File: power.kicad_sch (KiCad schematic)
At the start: 103 parts, among them Q1 BSS138AKA, Q2 SQS401EN-T1_BE3, Q3 DZDH0401DW, Q4 DMG1012T-7, Q5 DMG1012T-7, U3 LMR62014XMF, U4 AP62301_TSOT, U5 AP62301_TSOT, U6 AP22615A_TSOT26

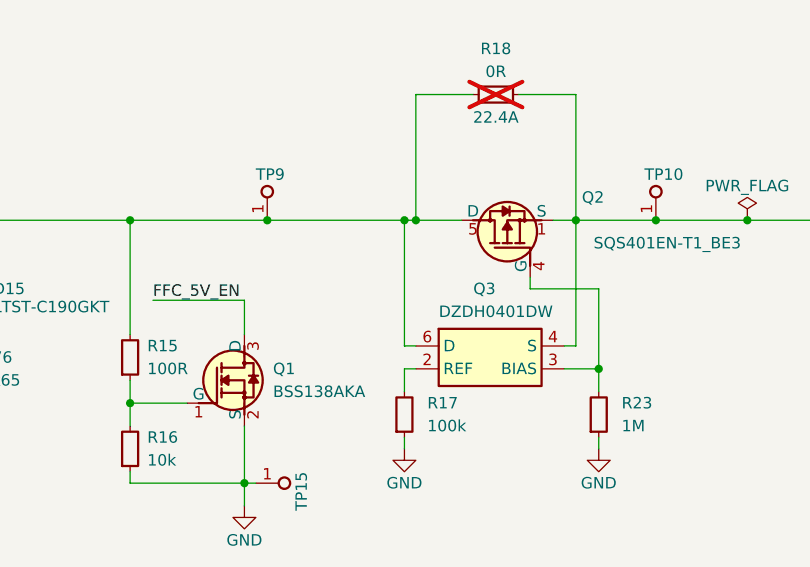
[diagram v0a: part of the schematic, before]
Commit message: [#74135] Update symbols and footprints
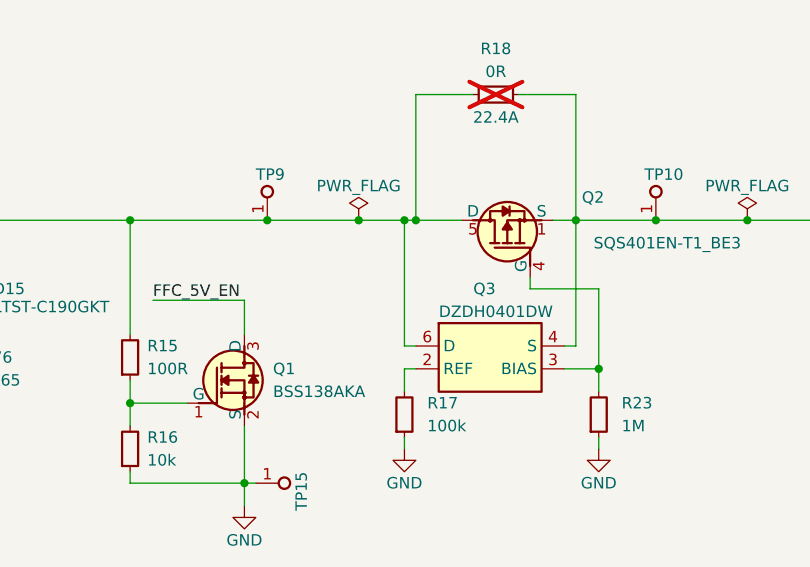
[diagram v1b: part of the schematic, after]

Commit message: [#74135] Fix DNP malformations
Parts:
- R18, R34: DNP DNP -> (none)
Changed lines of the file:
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@@
 			)
 		)
-		(property "DNP" "DNP"
-			(at 309.88 227.33 0)
-			(effects
-				(font
-					(size 1.27 1.27)
-				)
-				(hide yes)
-			)
-		)
 		(pin "1"
 		)
@@
 				(hide yes)
 			)
-		)
-		(property "DNP" "DNP"
-			(at 91.44 210.82 0)
-			(effects
-				(font
-					(size 1.27 1.27)
-				)
-				(hide yes)
-			)

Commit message: [#74135] Clean noInBom fields
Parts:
- Q4, Q5: now in the parts list
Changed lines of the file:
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@@
 	(label "FB_1V8"
 		(at 309.88 66.04 0)
-		(fields_autoplaced yes)
 		(effects
 			(font
@@
 	(label "FB_1V2"
 		(at 309.88 142.24 0)
-		(fields_autoplaced yes)
 		(effects
 			(font
@@
 	(label "EN_1V2"
 		(at 280.67 137.16 0)
-		(fields_autoplaced yes)
 		(effects
 			(font
@@
 	(label "FFC_5V_EN"
 		(at 347.98 222.25 0)
-		(fields_autoplaced yes)
 		(effects
 			(font
@@
 	(label "OUT_1V8"
 		(at 367.03 71.12 0)
-		(fields_autoplaced yes)
 		(effects
 			(font
@@
 	(label "FFC_5V_ISET"
 		(at 374.65 219.71 0)
-		(fields_autoplaced yes)
 		(effects
 			(font
@@
 	(label "SW_1V8"
 		(at 309.88 55.88 0)
-		(fields_autoplaced yes)
 		(effects
 			(font
@@
 	(label "EN_12V"
 		(at 189.23 238.76 0)
-		(fields_autoplaced yes)
 		(effects
 			(font
@@
 	(label "OUT_12V"
 		(at 238.76 232.41 0)
-		(fields_autoplaced yes)
 		(effects
 			(font
@@
 	(label "OUT_12V"
 		(at 275.59 240.03 270)
-		(fields_autoplaced yes)
 		(effects
 			(font
@@
 	(label "OUT_1V2"
 		(at 367.03 152.4 0)
-		(fields_autoplaced yes)
 		(effects
 			(font
@@
 	(label "EN_1V8"
 		(at 280.67 60.96 0)
-		(fields_autoplaced yes)
 		(effects
 			(font
@@
 	(label "FFC_5V_EN"
 		(at 326.39 223.52 180)
-		(fields_autoplaced yes)
 		(effects
 			(font
@@
 	(label "OUT_1V8"
 		(at 340.36 55.88 0)
-		(fields_autoplaced yes)
 		(effects
 			(font
@@
 	(label "SW_12V"
 		(at 214.63 232.41 0)
-		(fields_autoplaced yes)
 		(effects
 			(font
@@
 	(label "FB_12V"
 		(at 214.63 237.49 0)
-		(fields_autoplaced yes)
 		(effects
 			(font
@@
 	(label "OUT_1V2"
 		(at 340.36 132.08 0)
-		(fields_autoplaced yes)
 		(effects
 			(font
@@
 	(label "FFC_5V_EN"
 		(at 53.34 233.68 0)
-		(fields_autoplaced yes)
 		(effects
 			(font
@@
 	(label "SW_1V2"
 		(at 309.88 132.08 0)
-		(fields_autoplaced yes)
 		(effects
 			(font
@@
 	(label "FFC_5V_FLG"
 		(at 347.98 219.71 0)
-		(fields_autoplaced yes)
 		(effects
 			(font
@@
 		(shape input)
 		(at 330.2 217.17 180)
-		(fields_autoplaced yes)
 		(effects
 			(font
@@
 		(shape output)
 		(at 168.91 62.23 0)
-		(fields_autoplaced yes)
 		(effects
 			(font
@@
 		(shape input)
 		(at 309.88 215.9 90)
-		(fields_autoplaced yes)
 		(effects
 			(font
@@
 		(shape input)
 		(at 30.48 224.79 180)
-		(fields_autoplaced yes)
 		(effects
 			(font
@@
 		(shape output)
 		(at 168.91 140.97 0)
-		(fields_autoplaced yes)
 		(effects
 			(font
@@
 		(shape output)
 		(at 168.91 88.9 0)
-		(fields_autoplaced yes)
 		(effects
 			(font
@@
 		(shape output)
 		(at 168.91 114.3 0)
-		(fields_autoplaced yes)
 		(effects
 			(font
@@
 		(unit 1)
 		(exclude_from_sim no)
-		(in_bom no)
+		(in_bom yes)
 		(on_board yes)
 		(dnp no)
@@
 		(unit 1)
 		(exclude_from_sim no)
-		(in_bom no)
+		(in_bom yes)
 		(on_board yes)
 		(dnp no)

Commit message: [#80514] change 59S2AQ-40MT5-Z_1 connector to 7-2287906-0
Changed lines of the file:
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@@
 (kicad_sch
-	(version 20231120)
+	(version 20250114)
 	(generator "eeschema")
-	(generator_version "8.0")
+	(generator_version "9.0")
 	(paper "A3")
 	(title_block
@@
 		(comment 1 "www.antmicro.com")
 	)
+	(text "FFC 5V current limit"
+		(exclude_from_sim no)
+		(at 323.85 187.96 0)
+		(effects
+			(font
+				(size 4 4)
+				(thickness 0.8)
+				(bold yes)
+			)
+			(justify left bottom)
+		)
+	)
+	(text "Power arbiter"
+		(exclude_from_sim no)
+		(at 56.515 189.865 0)
+		(effects
+			(font
+				(size 4 4)
+				(thickness 0.8)
+				(bold yes)
+			)
+			(justify left bottom)
+		)
+	)
+	(text "Buck converter\n12V to 1.8V"
+		(exclude_from_sim no)
+		(at 294.64 28.575 0)
+		(effects
+			(font
+				(size 4 4)
+				(thickness 0.8)
+				(bold yes)
+			)
+			(justify left bottom)
+		)
+	)
+	(text "Boost converter\n5V to 12V"
+		(exclude_from_sim no)
+		(at 191.135 194.945 0)
+		(effects
+			(font
+				(size 4 4)
+				(thickness 0.8)
+				(bold yes)
+			)
+			(justify left bottom)
+		)
+	)
+	(text "Buck converter\n12V to 1.2V"
+		(exclude_from_sim no)
+		(at 294.64 105.41 0)
+		(effects
+			(font
+				(size 4 4)
+				(thickness 0.8)
+				(bold yes)
+			)
+			(justify left bottom)
+		)
+	)
+	(text "PoC circuit"
+		(exclude_from_sim no)
+		(at 94.615 37.465 0)
+		(effects
+			(font
+				(size 4 4)
+				(thickness 0.8)
+				(bold yes)
+			)
+			(justify left bottom)
+		)
+	)
 	(junction
 		(at 320.04 132.08)
@@
 		)
 	)
-	(text "FFC 5V current limit"
-		(exclude_from_sim no)
-		(at 323.85 187.96 0)
-		(effects
-			(font
-				(size 4 4)
-				(thickness 0.8)
-				(bold yes)
-			)
-			(justify left bottom)
-		)
-	)
-	(text "Power arbiter"
-		(exclude_from_sim no)
-		(at 56.515 189.865 0)
-		(effects
-			(font
-				(size 4 4)
-				(thickness 0.8)
-				(bold yes)
-			)
-			(justify left bottom)
-		)
-	)
-	(text "Buck converter\n12V to 1.8V"
-		(exclude_from_sim no)
-		(at 294.64 28.575 0)
-		(effects
-			(font
-				(size 4 4)
-				(thickness 0.8)
-				(bold yes)
-			)
-			(justify left bottom)
-		)
-	)
-	(text "Boost converter\n5V to 12V"
-		(exclude_from_sim no)
-		(at 191.135 194.945 0)
-		(effects
-			(font
-				(size 4 4)
-				(thickness 0.8)
-				(bold yes)
-			)
-			(justify left bottom)
-		)
-	)
-	(text "Buck converter\n12V to 1.2V"
-		(exclude_from_sim no)
-		(at 294.64 105.41 0)
-		(effects
-			(font
-				(size 4 4)
-				(thickness 0.8)
-				(bold yes)
-			)
-			(justify left bottom)
-		)
-	)
-	(text "PoC circuit"
-		(exclude_from_sim no)
-		(at 94.615 37.465 0)
-		(effects
-			(font
-				(size 4 4)
-				(thickness 0.8)
-				(bold yes)
-			)
-			(justify left bottom)
-		)
-	)

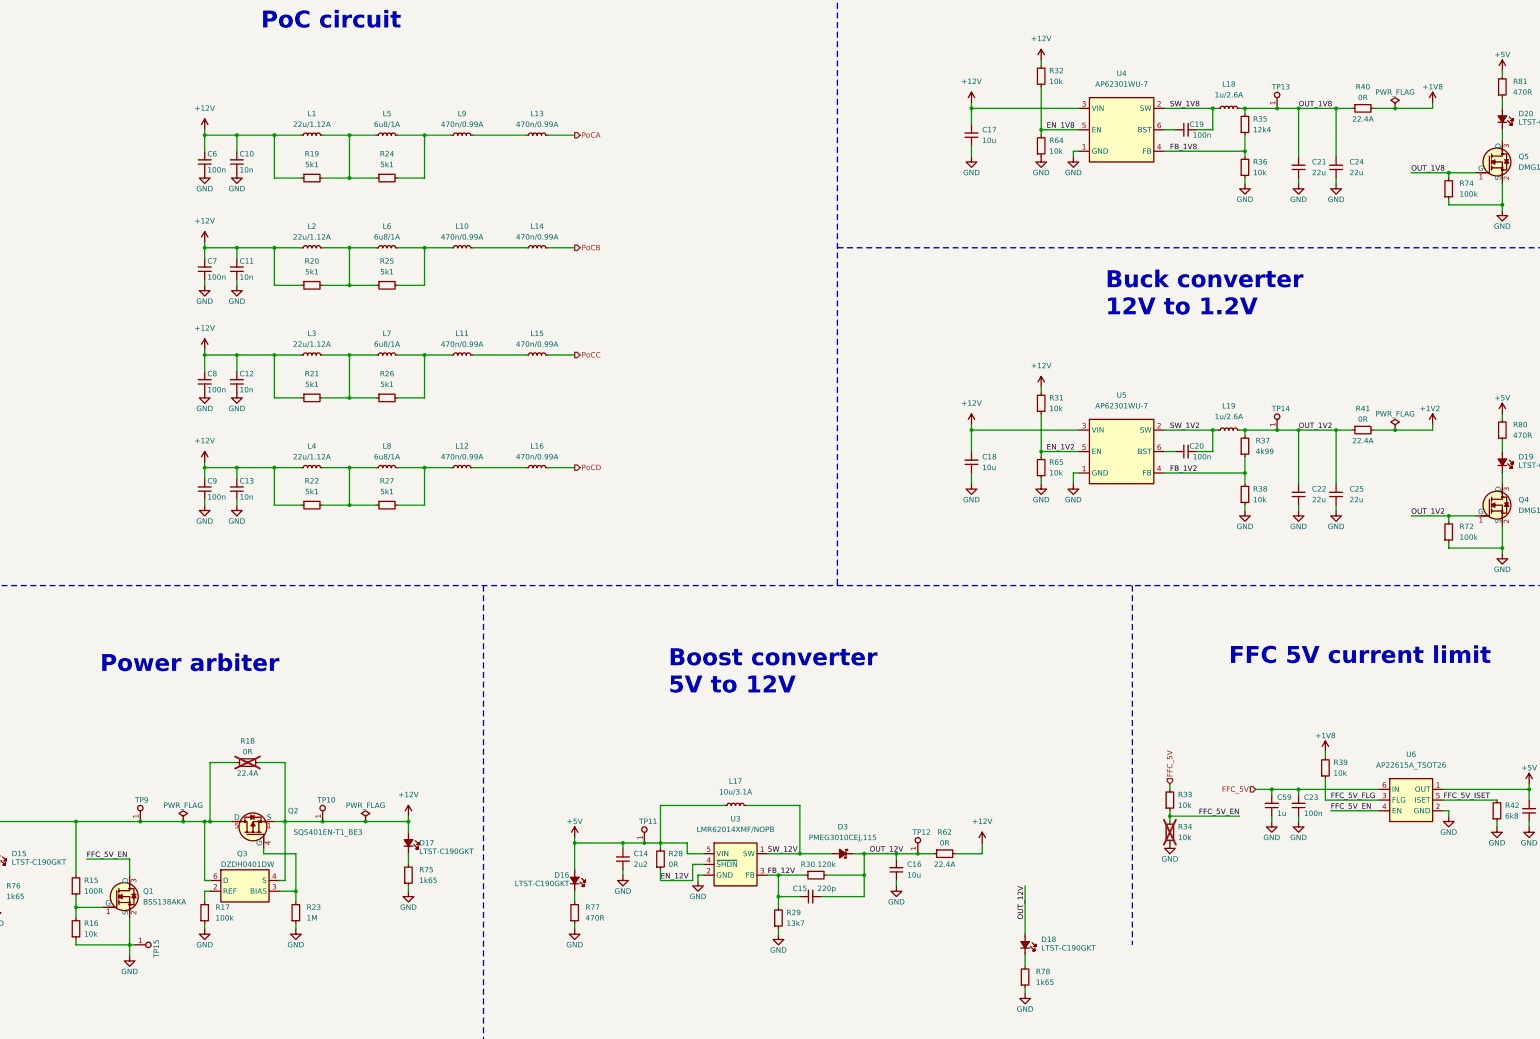
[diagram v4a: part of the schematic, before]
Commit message: [#80515] Add test points on OUT_1V8, 1V8, OUT 1V2, 1V2, 5V, FFC_5V, 12V, OUT_12V, FFC 3V3, DC_IN, DC_UNFUSED SDA, SCL, GND
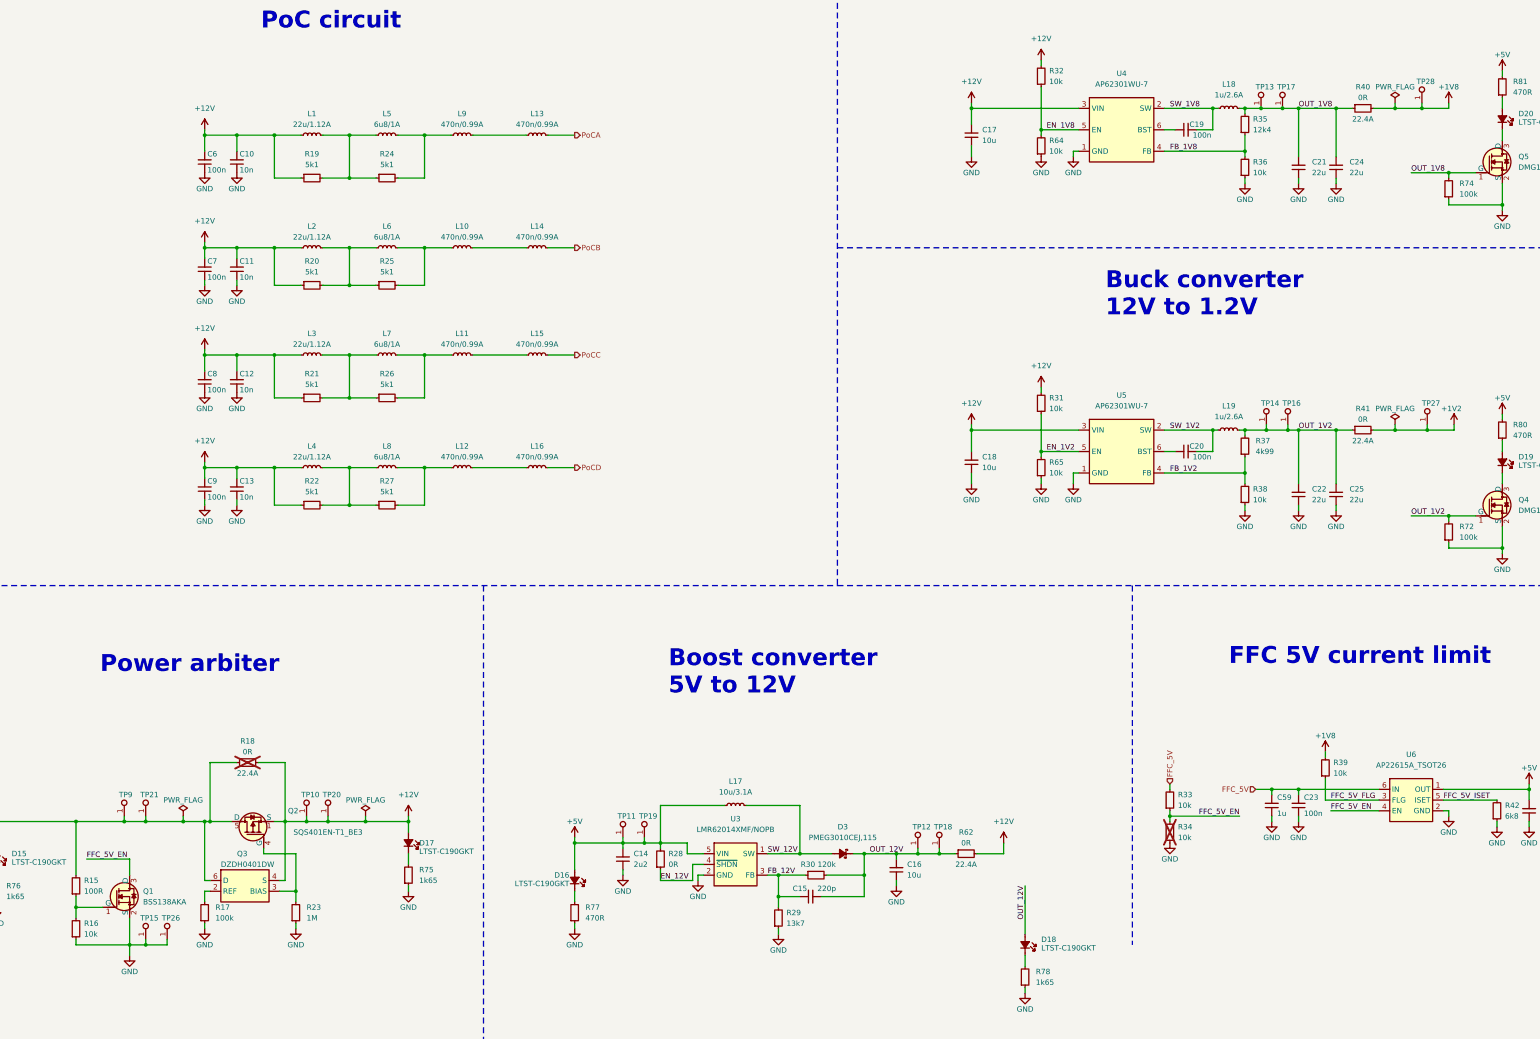
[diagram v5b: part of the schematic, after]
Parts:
- added TP16, TP17, TP18, TP19, TP20, TP21, TP26, TP27, TP28: TP_0.75mm_SMD, antmicro-footprints:TP_SMD_0.75mm, symbol antmicroTestPoints:TP_0.75mm_SMD
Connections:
- net +12V: now also TP20.1
- net +1V2: now also TP27.1
- net +1V8: now also TP28.1
- net +5V: now also TP19.1
- net DC_IN: now also TP21.1
- net GND: now also TP26.1
- net OUT_12V: now also TP18.1
- net OUT_1V2: now also TP16.1
- net OUT_1V8: now also TP17.1
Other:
- moved on the sheet: R62, TP10, TP11, TP12, TP13, TP14, TP15, TP9
